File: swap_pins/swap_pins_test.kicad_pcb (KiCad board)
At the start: 2 copper layers, 18 parts, among them U101 PIC18F452-IP, U201 PIC18F452-IP, U301 PIC18F452-IP

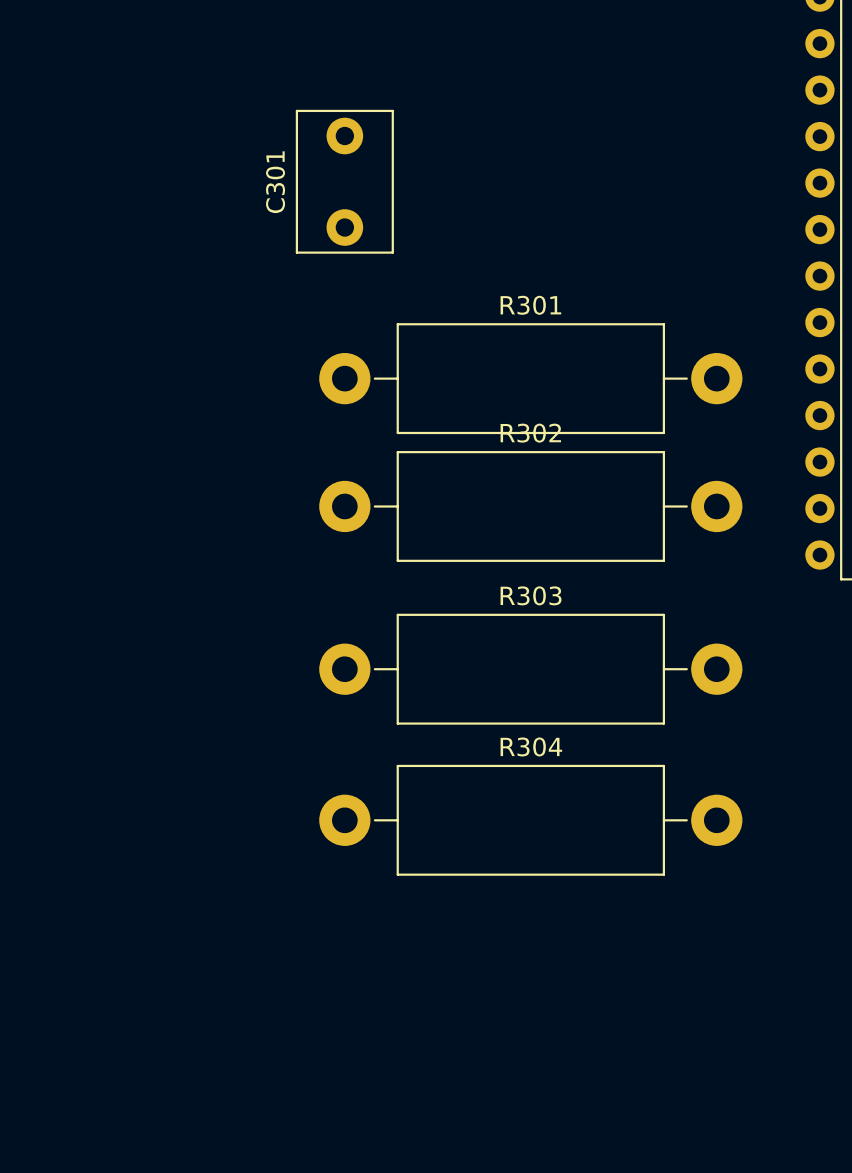
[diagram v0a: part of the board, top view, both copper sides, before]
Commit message: added global label test
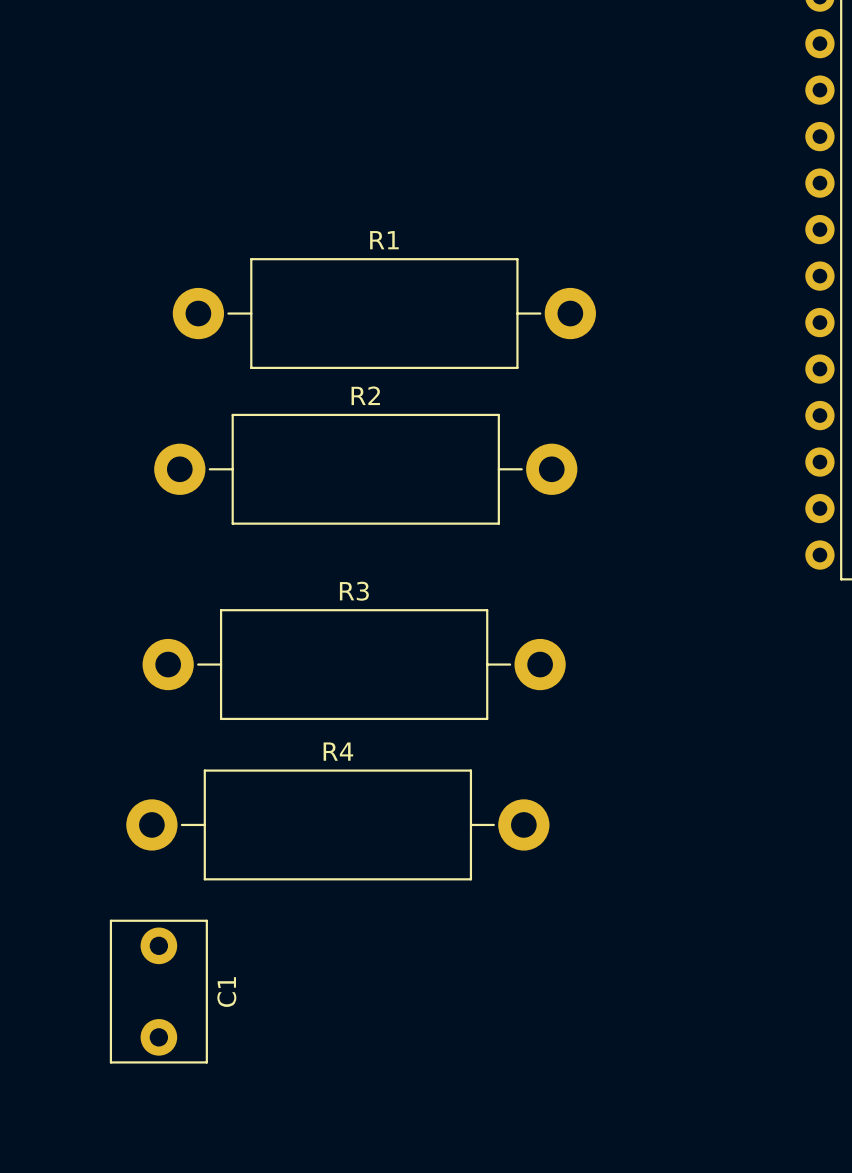
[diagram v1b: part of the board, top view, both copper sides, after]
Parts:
- removed C301: C, Capacitor_THT:C_Disc_D7.5mm_W5.0mm_P5.00mm
- removed R301, R302, R303, R304: R, Resistor_THT:R_Axial_DIN0614_L14.3mm_D5.7mm_P20.32mm_Horizontal
- added C1: C, Capacitor_THT:C_Disc_D7.5mm_W5.0mm_P5.00mm, F.Cu at (123.2, 106.6)
- added R1: R, Resistor_THT:R_Axial_DIN0614_L14.3mm_D5.7mm_P20.32mm_Horizontal, F.Cu at (125.3, 72.0)
- added R2: R, Resistor_THT:R_Axial_DIN0614_L14.3mm_D5.7mm_P20.32mm_Horizontal, F.Cu at (124.3, 80.5)
- added R3: R, Resistor_THT:R_Axial_DIN0614_L14.3mm_D5.7mm_P20.32mm_Horizontal, F.Cu at (123.7, 91.2)
- added R4: R, Resistor_THT:R_Axial_DIN0614_L14.3mm_D5.7mm_P20.32mm_Horizontal, F.Cu at (122.8, 99.9)
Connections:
- U301 pad 16: /level_1/Lavel_2/RC1 -> RC1
- U301 pad 17: /level_1/Lavel_2/RC2 -> RC2
- U301 pad 18: /level_1/Lavel_2/RC3 -> RC3
- U301 pad 23: /level_1/Lavel_2/RC4 -> RC4

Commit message: changed project to include hierarchical labels also
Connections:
- net /RB1 renamed RB1
- net /RB2 renamed RB2
- net /RB3 renamed RB3
- net /RB4 renamed RB4
- net RC1 renamed /level_1/Lavel_2/RC1
- net RC2 renamed /level_1/Lavel_2/RC2
- net RC3 renamed /level_1/Lavel_2/RC3
- net RC4 renamed /level_1/Lavel_2/RC4

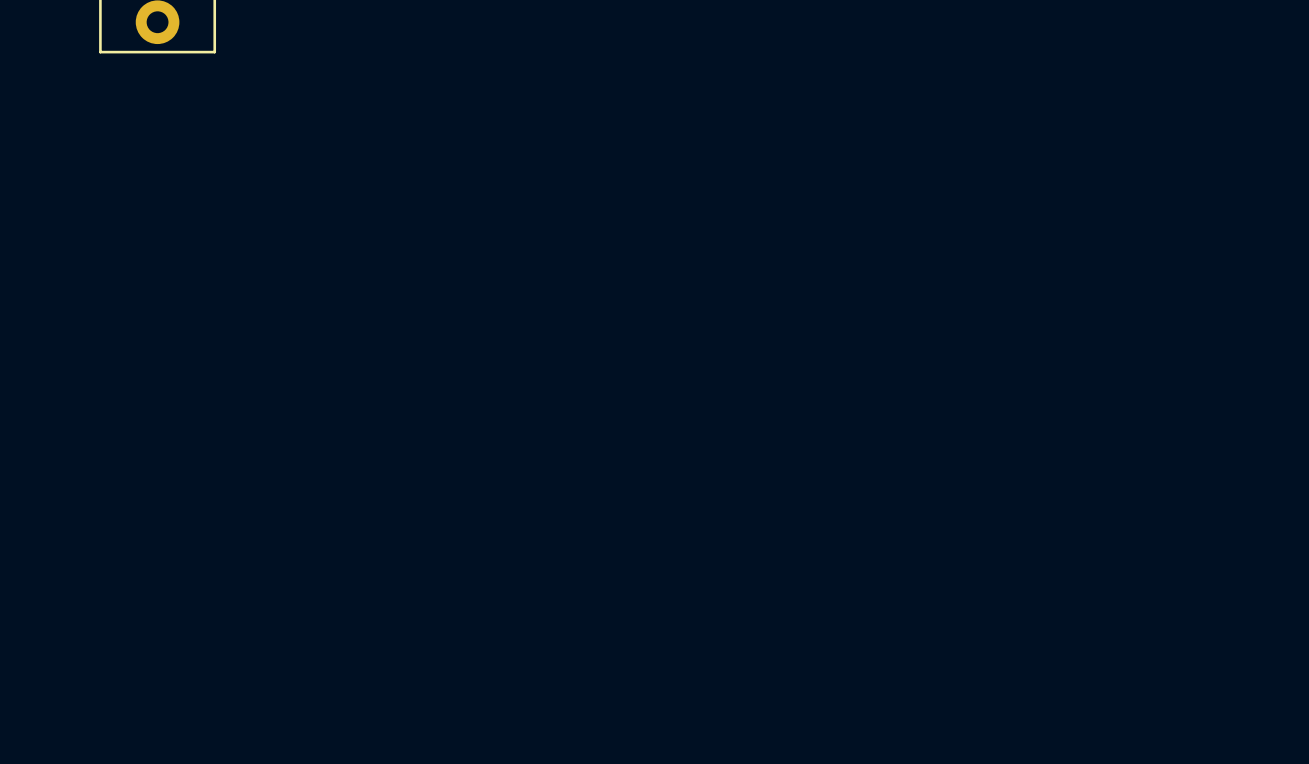
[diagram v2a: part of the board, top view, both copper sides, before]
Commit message: Overwritten the plugin with V2 version
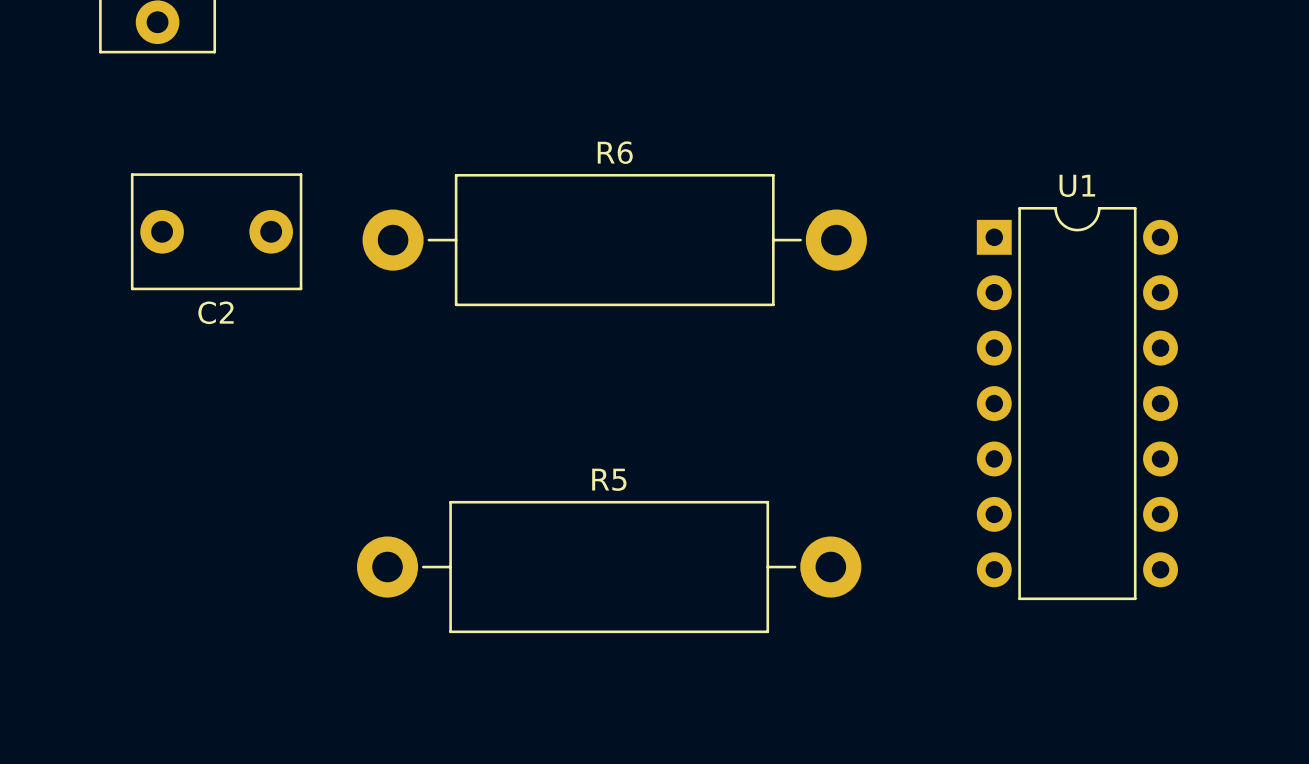
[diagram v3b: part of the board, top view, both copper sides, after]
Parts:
- added C2: C, Capacitor_THT:C_Disc_D7.5mm_W5.0mm_P5.00mm, F.Cu at (128.4, 121.2)
- added R5: R, Resistor_THT:R_Axial_DIN0614_L14.3mm_D5.7mm_P20.32mm_Horizontal, F.Cu at (133.7, 136.5)
- added R6: R, Resistor_THT:R_Axial_DIN0614_L14.3mm_D5.7mm_P20.32mm_Horizontal, F.Cu at (134.0, 121.5)
- added U1: LM324, Package_DIP:DIP-14_W7.62mm, F.Cu at (161.5, 121.4)
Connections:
- U101 pad 12: GND -> Net-(U101-Pad12)
